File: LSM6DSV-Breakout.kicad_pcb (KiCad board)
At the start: 2 copper layers, 16.5 x 20.3 mm, 16 parts, among them CN1 AFC10-S04QCA-00, CN2 AFC10-S04QCA-00, J1 Conn_01x06_Pin, J2 Conn_01x04_Pin, U1 LSM6DSVTR

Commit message: redo silkscreen
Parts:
- J1, J2: moved to B.Cu
- turned J1 to 180 degrees
- turned J2 to 180 degrees

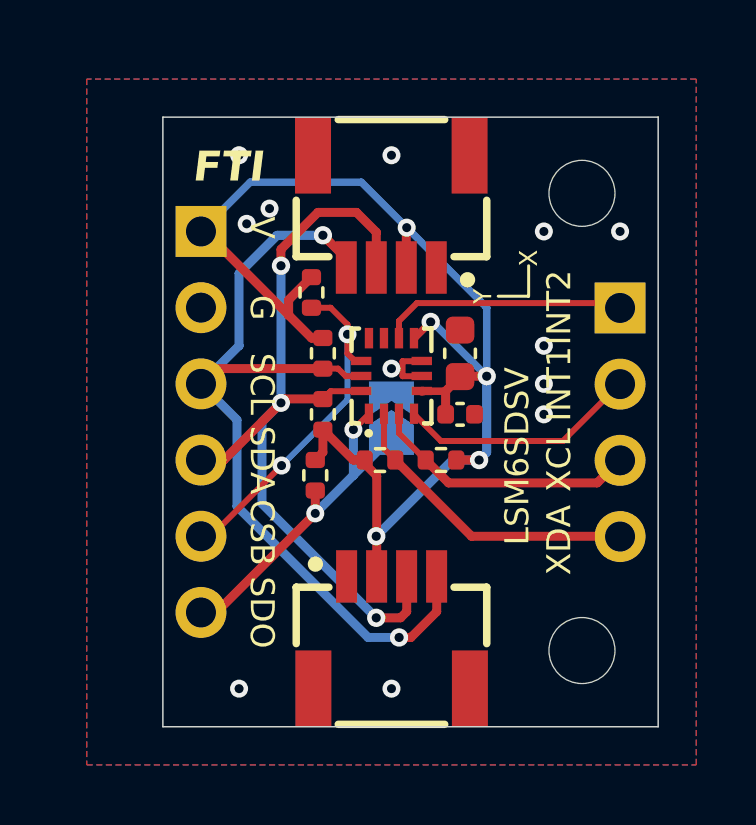
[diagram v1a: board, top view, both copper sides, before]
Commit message: use higher pullup, make dippable
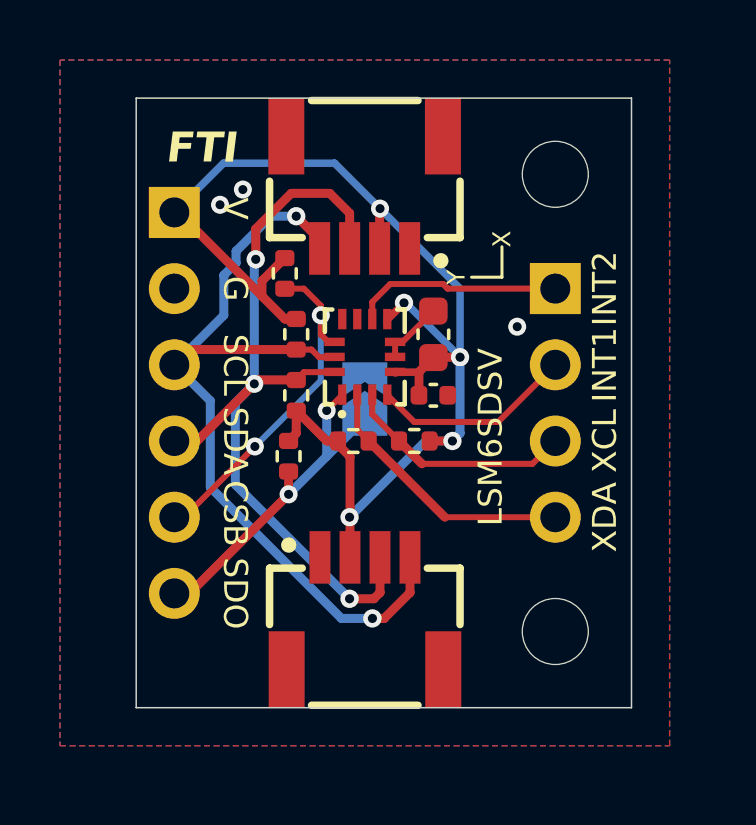
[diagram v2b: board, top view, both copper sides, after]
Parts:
- moved J2 2.25 mm to (66.0, 49.5)
- moved U1 1.09 mm to (59.7, 51.8)
- moved C1 1.09 mm to (62.0, 51.1)
- moved C2 1.09 mm to (62.0, 53.1)
- moved CN2 1.09 mm to (59.7, 60.4)
- moved JP1 1.09 mm to (59.7, 53.2)
- moved R2 1.09 mm to (57.1, 55.1)
- moved CN1 1.09 mm to (59.7, 46.3)
- moved H1 1.09 mm to (66.0, 61.0)
- moved H2 1.09 mm to (66.0, 45.7)
- moved J1 1.09 mm to (53.3, 47.0)
- moved R1 1.09 mm to (57.0, 49.0)
- moved R3 1.09 mm to (57.4, 53.1)
- moved R4 1.09 mm to (57.4, 51.1)
- moved R5 1.09 mm to (59.3, 54.6)
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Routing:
- net /INT2: track 8.26 -> 6.99 mm
- net /XDA: track 10.2 -> 8.96 mm
- net /XCL: track 9.01 -> 7.74 mm
- net /INT1: track 8.03 -> 6.76 mm
- net GND: track 2.99 -> 3.28 mm, vias 12 -> 3
